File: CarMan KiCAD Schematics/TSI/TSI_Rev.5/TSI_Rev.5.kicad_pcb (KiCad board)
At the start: 2 copper layers, 203.2 x 165.1 mm, 255 parts, among them IC1 TS431ILT, IC4 TS431ILT, J1 J1, J10 J10, J11 J11, J12 J12, J13 Conn_01x01, J13.1 Conn_01x06, J13.2 Conn_01x06, J14 J14, J15 J15, J16 J16, J17 J17, J18 J18, J19 J19, J2 Current_Sensor, J20 J20, J21 J21, J22 J22, J23 J23, J24 Conn_01x01, J25 Conn_01x01, J26 J26, J27 J27, J28 Conn_01x01, J29 J29, J3 J3, J4 J4, J5 J5, J6 J6, J7 J7, J8 J8, J9 J9, K1 APAN3105, K2 G5LE-1-E, K3 SFS2-DC24V, K4 SFS2-DC24V, Q1 ZVP1320F, Q11 TN2130K1-G, Q2 MMBF170, Q3 ZVP1320F, Q5 SI1302DL-T1-E3, SW1 TS5A3159DBVT, U1 RDE03110S12, U10 MC7805BDTRKG, U11 TLP293, U12 REF3033, U13 TLP293, U14 Bottom Left, U15 Top Left, U16 TS372CDT, U17 Top Right, U18 MCP6004, U19 74HC00, U2 Bottom Right, U21 MCP6004, U22 MCP23016-I_SO, U23 DAC5574IDGS, U24 TLP293, U25 NCD9830DBR2G, U26 MCP6004, U29 SN74LVC1G08DCKR, U3 TS912, U30 TLP293, U31 TLP293, U32 TLP293, U34 TLP293, U35 MCP6004, U37 TLP293, U4 ACPL-C870, U40 MCP6004, U41 PDQ10-Q24-D5-D, U42 LT1763CS8-3.3PBF, U48 TLP293, U49 TLP293, U5 SI8600AB-B-IS, U6 TS912, U7 MCP6004, U8 74ACT11030, U9 STN3NF06L

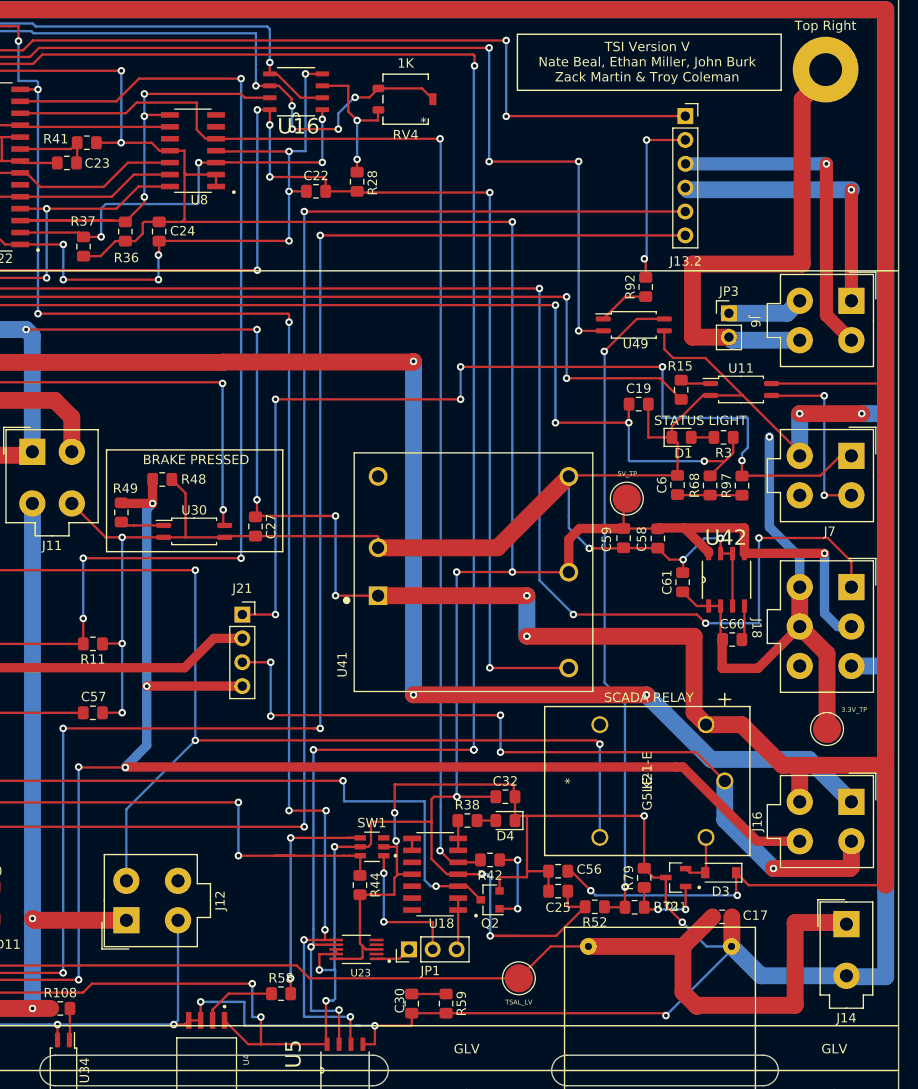
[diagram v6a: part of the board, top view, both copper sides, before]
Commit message: Updated Signals and Trace Width
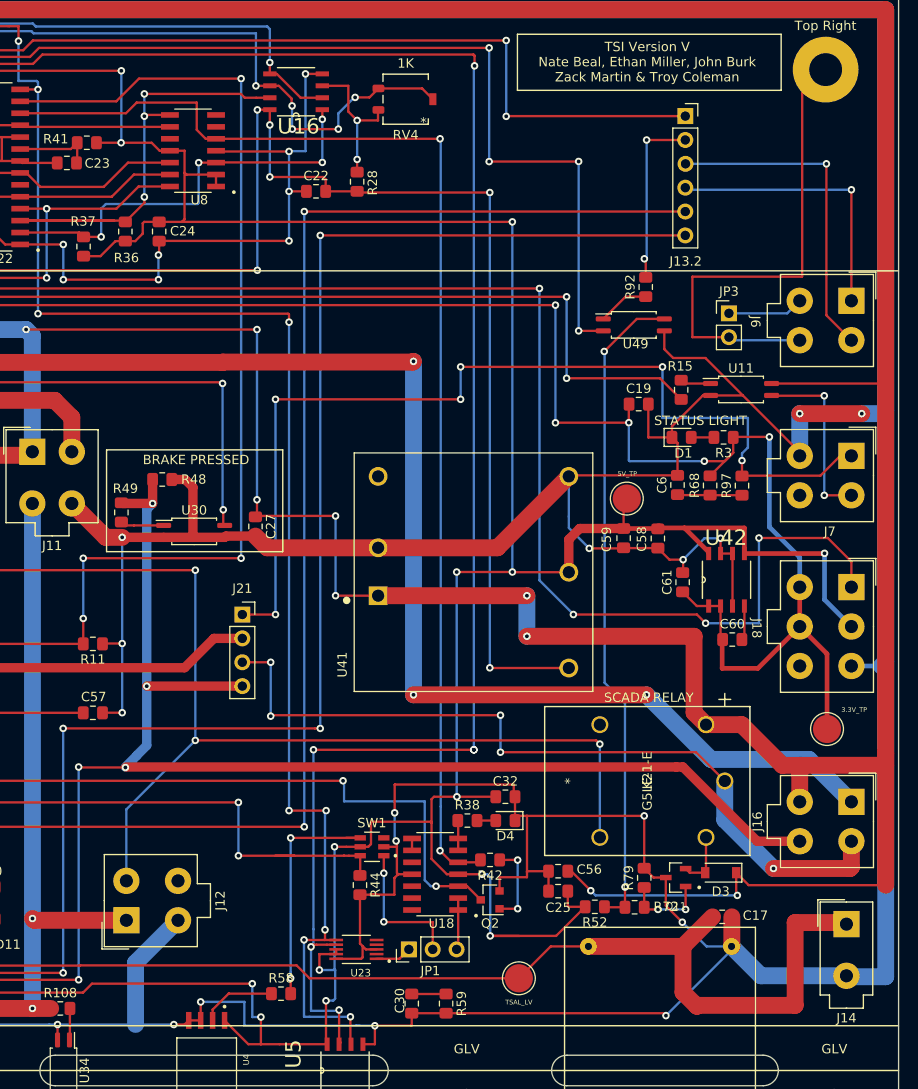
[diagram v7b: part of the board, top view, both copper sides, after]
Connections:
- net /Cooling_power renamed /CAN_GLV_POWER/Cooling_power
- J4 pad 1: /IGNI_GND -> /DC_RELAY-
- JP2 pad 2: /IGNI_GND -> /DC_RELAY-
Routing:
- net /DC_RELAY-: track 411.0 -> 444.2 mm
- net /IGNI_GND: track 33.3 -> 0.00 mm
- net /3.3V: track 311.7 -> 315.5 mm
- net /AIRS-: track 1477.1 -> 1479.3 mm
- net /Chassis_GND: track 53.8 -> 52.8 mm
- net /5V: track 542.9 -> 542.0 mm

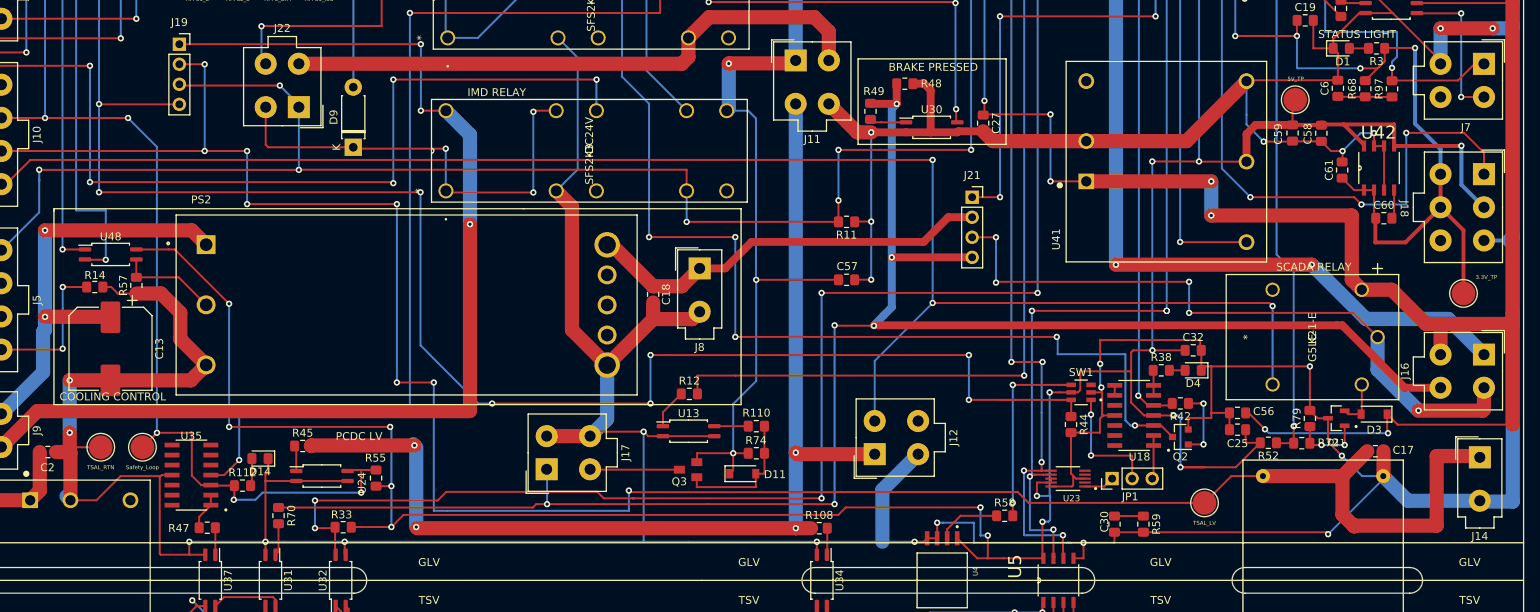
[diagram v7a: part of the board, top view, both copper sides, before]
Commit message: Updated trace width and connector naming
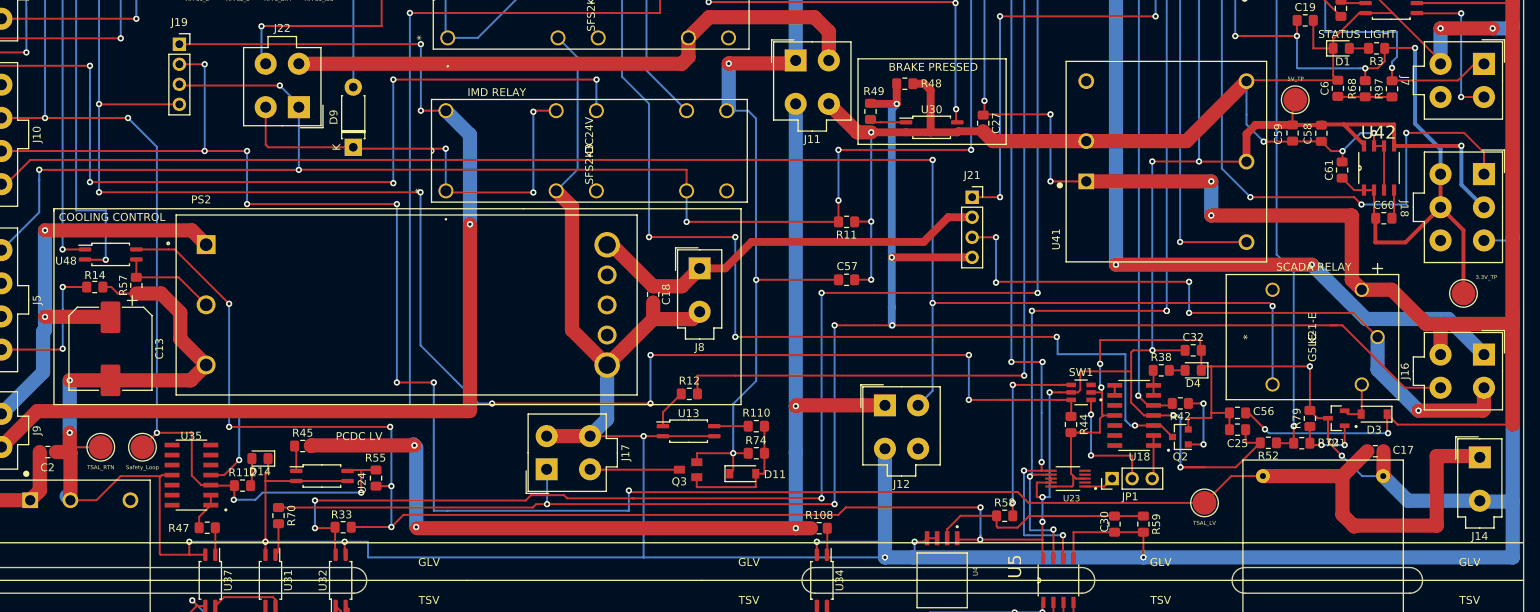
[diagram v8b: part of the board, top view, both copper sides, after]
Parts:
- moved J12 6.32 mm to (222.5, 145.0), turned to 0 degrees
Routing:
- net /AIRS-: track 1479.3 -> 1524.1 mm, vias 38 -> 37
- net Net-(C30-Pad1): track 11.8 -> 28.7 mm
- net /5V: track 542.0 -> 536.9 mm
- net /GEN_Fault_LED: track 208.5 -> 204.3 mm
- net /3.3V: track 315.5 -> 313.6 mm
- net /Brake_Light: track 224.4 -> 223.1 mm
- net /AIRS+: track 137.8 -> 139.0 mm
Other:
- board text added: "J7"
